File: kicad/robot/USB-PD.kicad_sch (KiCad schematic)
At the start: 36 parts, among them U11 MAX77958EWV+T

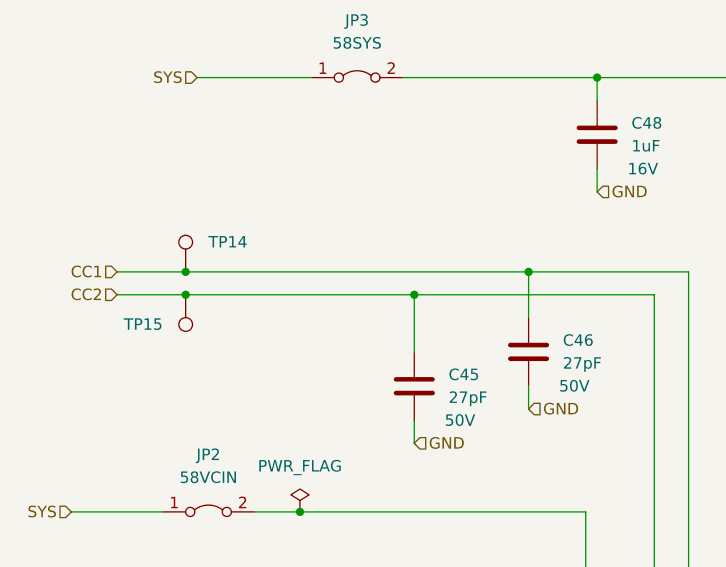
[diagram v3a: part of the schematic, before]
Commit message: removed two additional duplicate test points
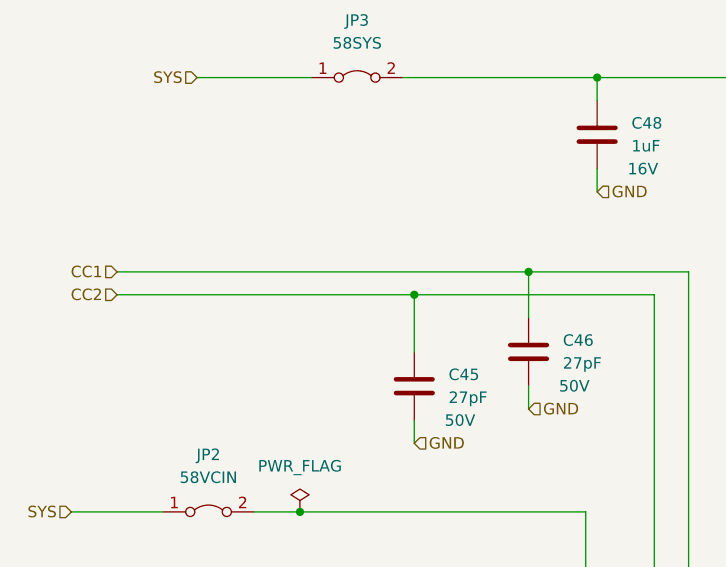
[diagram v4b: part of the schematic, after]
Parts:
- removed TP14, TP15: TestPoint, symbol Connector:TestPoint
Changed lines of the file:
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@@
   (junction (at 223.52 204.47) (diameter 0) (color 0 0 0 0)
   )
-  (junction (at 179.07 161.29) (diameter 0) (color 0 0 0 0)
-  )
   (junction (at 356.87 264.16) (diameter 0) (color 0 0 0 0)
   )
@@
   )
   (junction (at 342.9 264.16) (diameter 0) (color 0 0 0 0)
-  )
-  (junction (at 179.07 158.75) (diameter 0) (color 0 0 0 0)
   )
   (junction (at 321.31 204.47) (diameter 0) (color 0 0 0 0)
@@
     (stroke (width 0) (type default) (color 0 0 0 0))
   )
-  (wire (pts (xy 179.07 158.75) (xy 217.17 158.75))
+  (wire (pts (xy 171.45 158.75) (xy 217.17 158.75))
     (stroke (width 0) (type default) (color 0 0 0 0))
   )
@@
     (stroke (width 0) (type default) (color 0 0 0 0))
   )
-  (wire (pts (xy 171.45 158.75) (xy 179.07 158.75))
-    (stroke (width 0) (type default) (color 0 0 0 0))
-  )
   (wire (pts (xy 316.23 167.64) (xy 316.23 161.29))
     (stroke (width 0) (type default) (color 0 0 0 0))
@@
     (stroke (width 0) (type default) (color 0 0 0 0))
   )
-  (wire (pts (xy 179.07 161.29) (xy 204.47 161.29))
+  (wire (pts (xy 171.45 161.29) (xy 204.47 161.29))
     (stroke (width 0) (type default) (color 0 0 0 0))
   )
@@
   )
   (wire (pts (xy 290.83 276.86) (xy 290.83 279.4))
-    (stroke (width 0) (type default) (color 0 0 0 0))
-  )
-  (wire (pts (xy 171.45 161.29) (xy 179.07 161.29))
     (stroke (width 0) (type default) (color 0 0 0 0))
   )
@@
     (pin "1")
     (pin "2")
-  )
-  (symbol (lib_id "Connector:TestPoint") (at 179.07 158.75 0) (unit 1)
-    (in_bom yes) (on_board yes) (fields_autoplaced)
-    (property "Reference" "TP14" (id 0) (at 181.61 155.4479 0)
-      (effects (font (size 1.27 1.27)) (justify left))
-    )
-    (property "Value" "TestPoint" (id 1) (at 181.61 156.7179 0)
-      (effects (font (size 1.27 1.27)) (justify left) hide)
-    )
-    (property "Footprint" "" (id 2) (at 184.15 158.75 0)
-      (effects (font (size 1.27 1.27)) hide)
-    )
-    (property "Datasheet" "~" (id 3) (at 184.15 158.75 0)
-      (effects (font (size 1.27 1.27)) hide)
-    )
-    (pin "1")
   )
   (symbol (lib_id "Jumper:Jumper_2_Bridged") (at 382.27 194.31 0) (unit 1)
@@
     (pin "2")
   )
-  (symbol (lib_id "Connector:TestPoint") (at 179.07 161.29 0) (mirror x) (unit 1)
-    (in_bom yes) (on_board yes) (fields_autoplaced)
-    (property "Reference" "TP15" (id 0) (at 176.53 164.5919 0)
-      (effects (font (size 1.27 1.27)) (justify right))
-    )
-    (property "Value" "TestPoint" (id 1) (at 176.53 165.8619 0)
-      (effects (font (size 1.27 1.27)) (justify right) hide)
-    )
-    (property "Footprint" "" (id 2) (at 184.15 161.29 0)
-      (effects (font (size 1.27 1.27)) hide)
-    )
-    (property "Datasheet" "~" (id 3) (at 184.15 161.29 0)
-      (effects (font (size 1.27 1.27)) hide)
-    )
-    (pin "1")
-  )
   (symbol (lib_id "Jumper:Jumper_2_Bridged") (at 222.25 114.3 0) (unit 1)

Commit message: Added keystone test points
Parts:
- TP16, TP17, TP18, TP19, TP20, TP21, TP22: footprint (none) -> TestPoint:KEYSTONE_5002
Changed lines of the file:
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@@
       (effects (font (size 1.27 1.27)) (justify right) hide)
     )
-    (property "Footprint" "" (id 2) (at 316.23 201.93 0)
+    (property "Footprint" "TestPoint:KEYSTONE_5002" (id 2) (at 316.23 201.93 0)
       (effects (font (size 1.27 1.27)) hide)
     )
@@
       (effects (font (size 1.27 1.27)) (justify right) hide)
     )
-    (property "Footprint" "" (id 2) (at 311.15 219.71 0)
+    (property "Footprint" "TestPoint:KEYSTONE_5002" (id 2) (at 311.15 219.71 0)
       (effects (font (size 1.27 1.27)) hide)
     )
@@
       (effects (font (size 1.27 1.27)) (justify right) hide)
     )
-    (property "Footprint" "" (id 2) (at 337.82 218.44 0)
+    (property "Footprint" "TestPoint:KEYSTONE_5002" (id 2) (at 337.82 218.44 0)
       (effects (font (size 1.27 1.27)) hide)
     )
@@
       (effects (font (size 1.27 1.27)) (justify right) hide)
     )
-    (property "Footprint" "" (id 2) (at 355.6 194.31 0)
+    (property "Footprint" "TestPoint:KEYSTONE_5002" (id 2) (at 355.6 194.31 0)
       (effects (font (size 1.27 1.27)) hide)
     )
@@
       (effects (font (size 1.27 1.27)) (justify right) hide)
     )
-    (property "Footprint" "" (id 2) (at 316.23 204.47 0)
+    (property "Footprint" "TestPoint:KEYSTONE_5002" (id 2) (at 316.23 204.47 0)
       (effects (font (size 1.27 1.27)) hide)
     )
@@
       (effects (font (size 1.27 1.27)) (justify right) hide)
     )
-    (property "Footprint" "" (id 2) (at 311.15 222.25 0)
+    (property "Footprint" "TestPoint:KEYSTONE_5002" (id 2) (at 311.15 222.25 0)
       (effects (font (size 1.27 1.27)) hide)
     )
@@
       (effects (font (size 1.27 1.27)) (justify right) hide)
     )
-    (property "Footprint" "" (id 2) (at 355.6 229.87 0)
-      (effects (font (size 1.27 1.27)) hide)
-    )
+    (property "Footprint" "TestPoint:KEYSTONE_5002" (id 2) (at 355.6 229.87 0)
+      (effects (font (size 1.27 1.27)) hide)
+    )
